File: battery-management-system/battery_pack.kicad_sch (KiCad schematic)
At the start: 23 parts, among them J1 CELL4_PLUS, J10 VBAT+_CHARGE, J2 CELL4_MINUS, J3 CELL3_MINUS, J4 CELL2_MINUS, J5 CELL1_MINUS, J6 VBAT+, J8 VBAT-, Q1 DMN3730U, Q2 TJ40S04M3L, Q3 TJ40S04M3L, Q4 DMN3730U

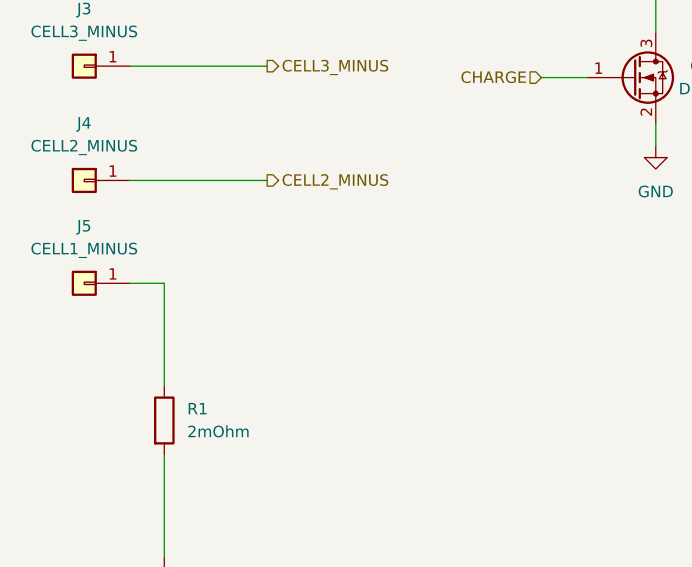
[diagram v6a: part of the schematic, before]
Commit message: add balancing sheet
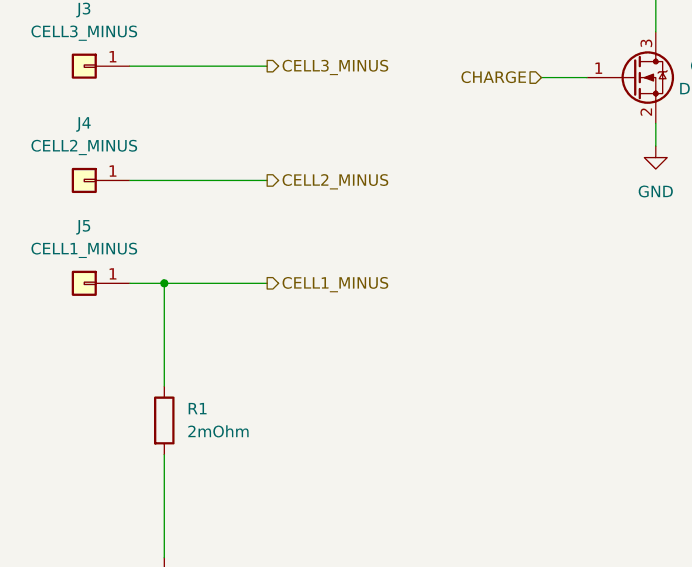
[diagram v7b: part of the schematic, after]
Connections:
- net CELL1_MINUS: now reaches J5.1 (Pin_1), R1.1
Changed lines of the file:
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@@
 (kicad_sch (version 20230121) (generator eeschema)
   (paper "A4")
+  (junction (at 40.64 113.03) (diameter 0) (color 0 0 0 0)
+  )
   (junction (at 207.01 86.36) (diameter 0) (color 0 0 0 0)
   )
@@
   )
   (wire (pts (xy 85.09 44.45) (xy 48.26 44.45))
+    (stroke (width 0) (type default))
+  )
+  (wire (pts (xy 40.64 113.03) (xy 52.07 113.03))
     (stroke (width 0) (type default))
   )
@@
     (effects (font (size 1.27 1.27)) (justify left))
   )
+  (hierarchical_label "CELL1_MINUS" (shape output) (at 52.07 113.03 0) (fields_autoplaced)
+    (effects (font (size 1.27 1.27)) (justify left))
+  )

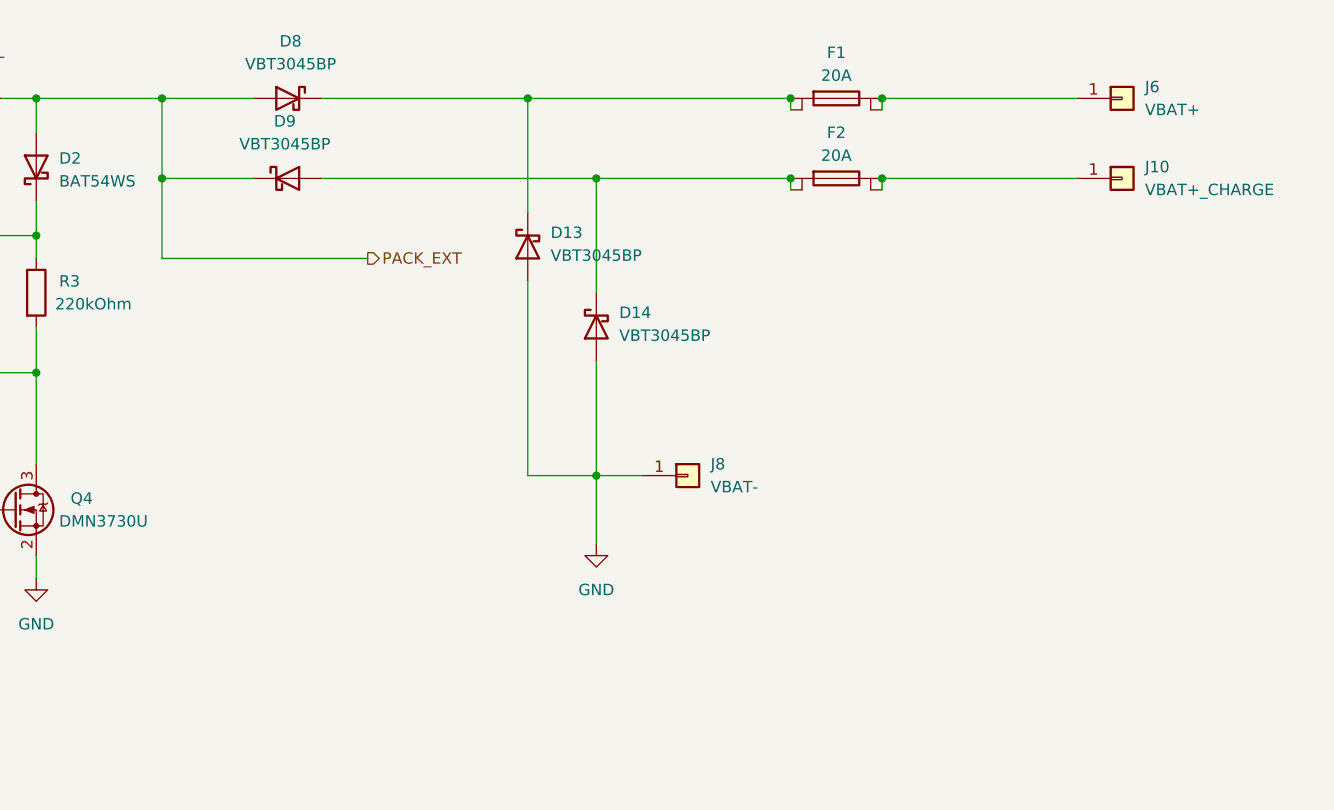
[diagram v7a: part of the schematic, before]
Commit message: implement balancing
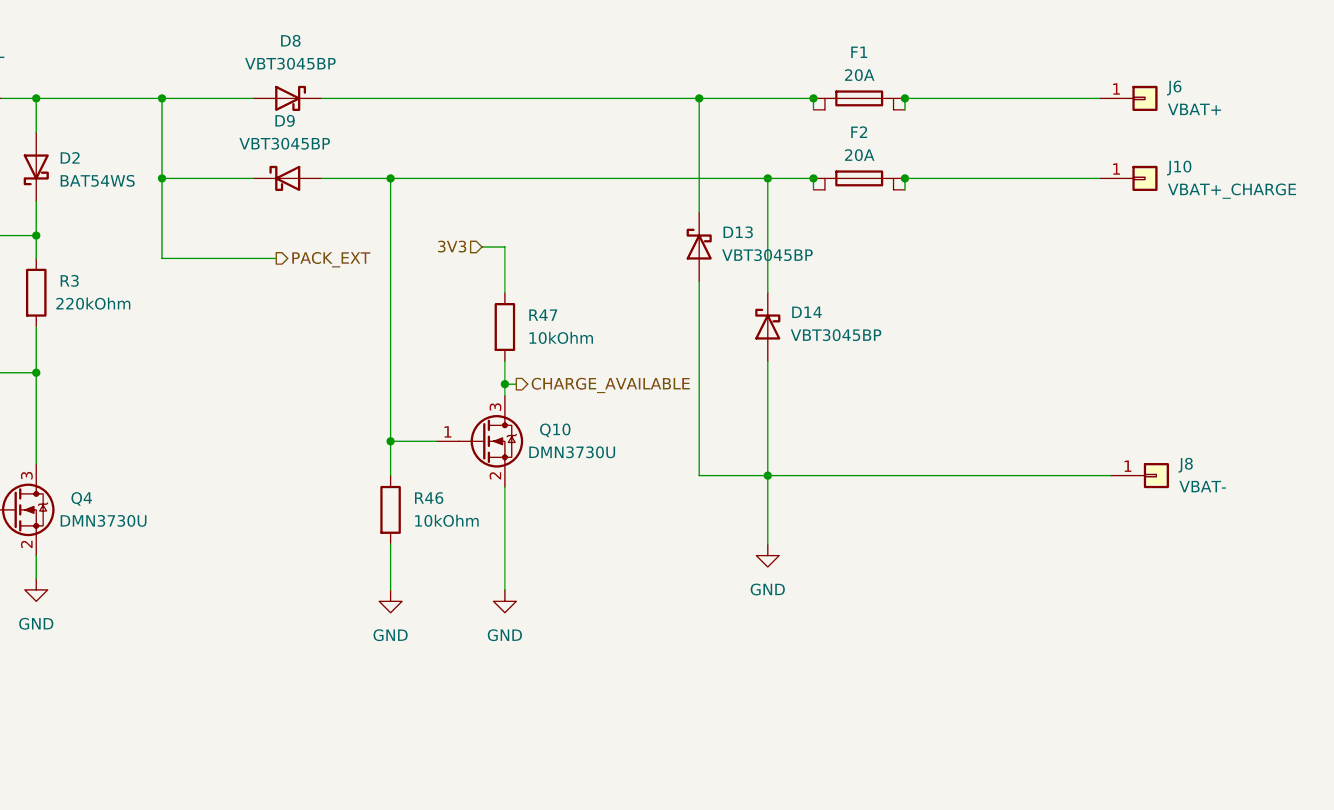
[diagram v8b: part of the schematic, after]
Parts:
- added Q10: DMN3730U, benediktibk:SOT-23, symbol benediktibk:DMN3730U
- added R46, R47: 10kOhm, benediktibk:R_0603_1608Metric_Pad0.98x0.95mm_HandSolder, symbol benediktibk:R_10kOhm_SMD_0603_100mW_1%
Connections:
- net GND: now also Q10.2 (S), R46.2
- net at D14.2 (K), D9.2 (K), F2.3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: now also Q10.1 (G), R46.1
- new net 3V3: R47.1
- new net CHARGE_AVAILABLE: Q10.3 (D), R47.2
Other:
- moved on the sheet: D13, D14, F1, F2, J10, J6, J8
